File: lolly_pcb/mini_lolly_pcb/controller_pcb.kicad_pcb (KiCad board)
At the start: 2 copper layers, 94 x 94 mm, 66 parts

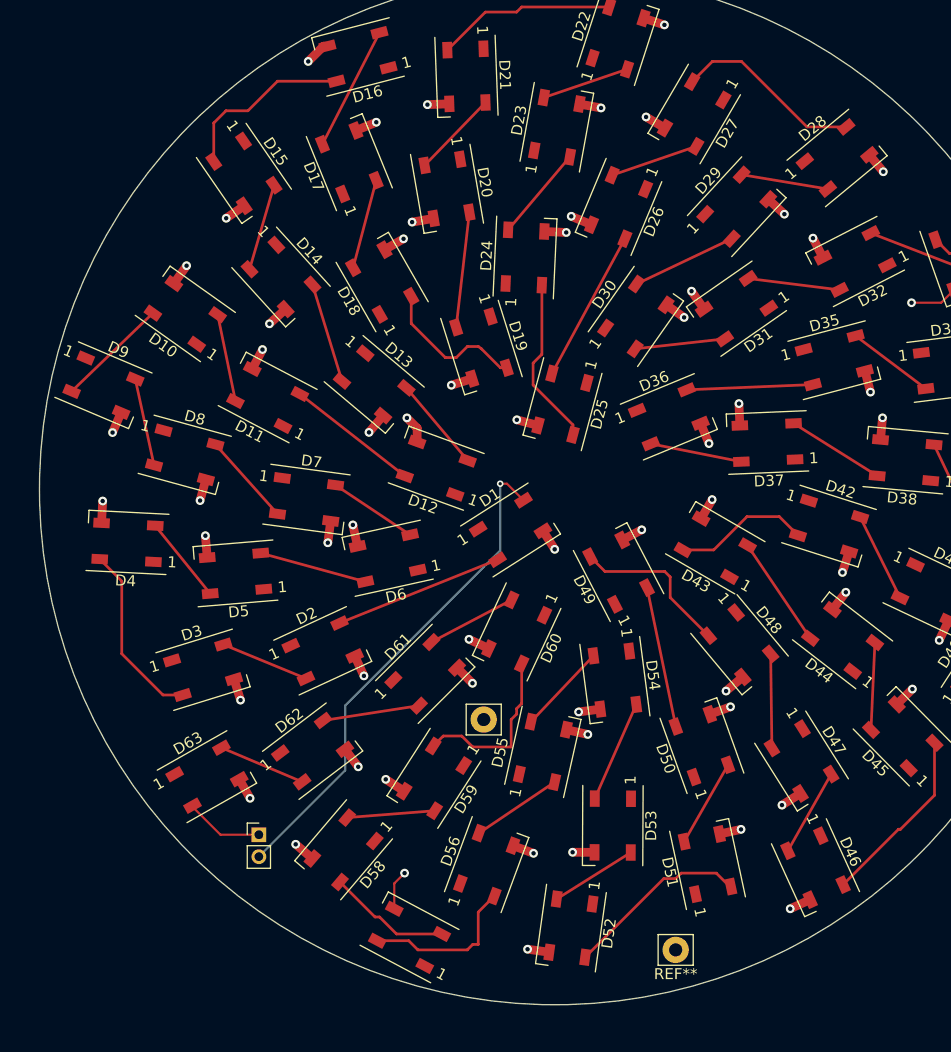
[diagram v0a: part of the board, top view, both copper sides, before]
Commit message: add esp32 s3-mini as controller
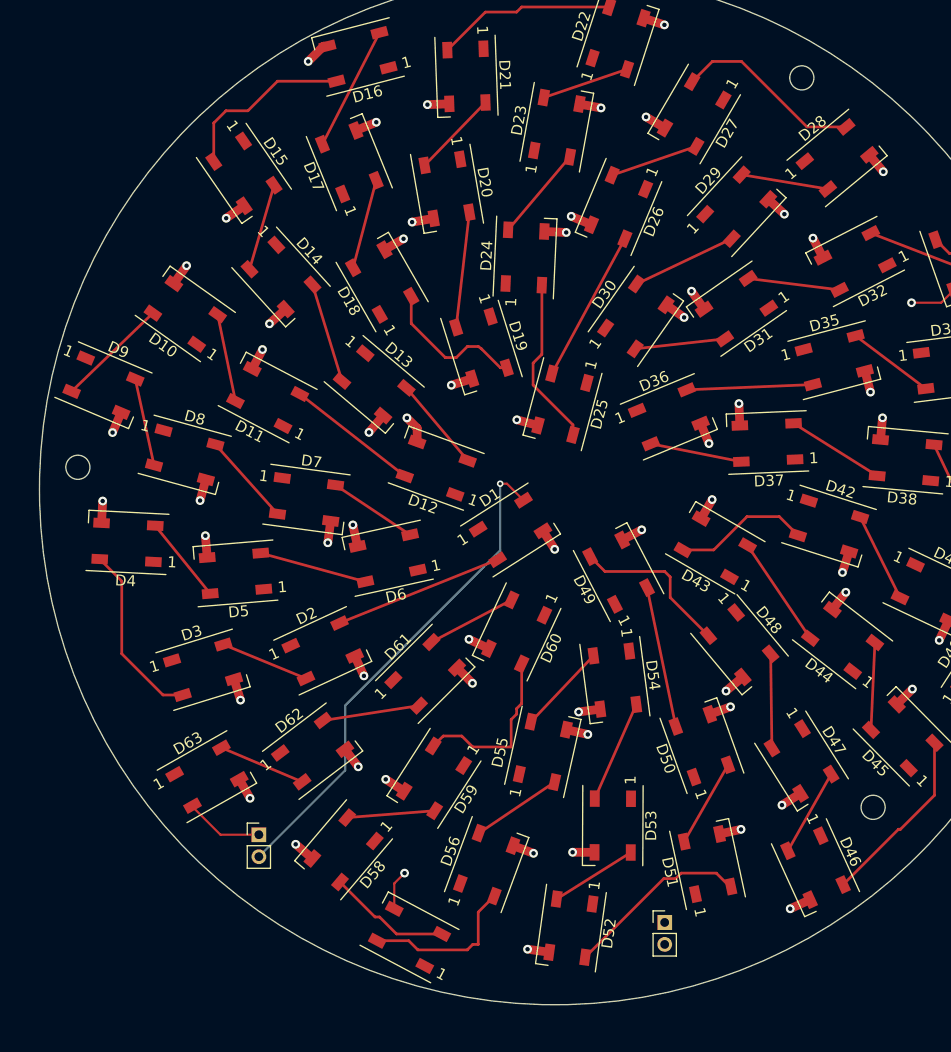
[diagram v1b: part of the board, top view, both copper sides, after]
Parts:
- removed the REF** at (161.0, 142.0)
- removed the REF** at (143.5, 121.0)
- added REF**: PinHeader_1x02_P2.00mm_Vertical, Connector_PinHeader_2.00mm:PinHeader_1x02_P2.00mm_Vertical, F.Cu at (160.0, 139.5)
- added REF**: MountingHole_2.2mm_M2, MountingHole:MountingHole_2.2mm_M2, F.Cu at (172.5, 62.5)
- added REF**: MountingHole_2.2mm_M2, MountingHole:MountingHole_2.2mm_M2, F.Cu at (179.0, 129.0)
- added REF**: MountingHole_2.2mm_M2, MountingHole:MountingHole_2.2mm_M2, F.Cu at (106.5, 98.0)
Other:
- board text added: "Mini Lolly V1"
